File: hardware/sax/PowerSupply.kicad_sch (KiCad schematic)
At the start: 8 parts, among them U1201 TPSM33625

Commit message: Update library
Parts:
- C1201: footprint Capacitor_SMD:C_1210_3225Metric -> V2_Capacitor_SMD:C_1210; symbol Device:C_Small -> V2_Device:C_1210_10u; Manufacturer (none) -> TDK; Mouser (none) -> 810-CNA6P1X7R1H106K2; Product (none) -> CNA6P1X7R1H106K250AE; Voltage (none) -> 50V
- C1202: footprint Capacitor_SMD:C_0603_1608Metric -> V2_Capacitor_SMD:C_0603; symbol Device:C_Small -> V2_Device:C_0603_0u1; Manufacturer (none) -> TDK; Mouser (none) -> 810-CGA3E2X7R1H104MA; Product (none) -> CGA3E2X7R1H104M080AA
- C1203, C1204: footprint Capacitor_SMD:C_1210_3225Metric -> V2_Capacitor_SMD:C_1210; symbol Device:C_Small -> V2_Device:C_1210_22u; Manufacturer (none) -> TDK; Mouser (none) -> 810-CGA6P3X7R1E226M5; Product (none) -> CGA6P3X7R1E226M250AE; Voltage (none) -> 25V
- C1205: footprint Capacitor_SMD:C_0603_1608Metric -> V2_Capacitor_SMD:C_0603; symbol Device:C_Small -> V2_Device:C_0603_1u; Manufacturer (none) -> YAGEO; Mouser (none) -> 603-CC603KRX7R9BB105; Product (none) -> CC0603KRX7R9BB105
- R1201: footprint Resistor_SMD:R_0603_1608Metric -> V2_Resistor_SMD:R_0603; symbol Device:R_Small -> V2_Device:R_0603_40k2; Manufacturer (none) -> Vishay; Mouser (none) -> 71-RCS060340K2FKEA; Product (none) -> RCS060340K2FKEA; Rating (none) -> 500mW
- R1202: footprint Resistor_SMD:R_0603_1608Metric -> V2_Resistor_SMD:R_0603; symbol Device:R_Small -> V2_Device:R_0603_10k; Manufacturer (none) -> Vishay; Mouser (none) -> 71-CRCW060310K0FKEAC; Product (none) -> CRCW060310K0FKEAC; Rating (none) -> 100mW
- U1201: Manufacturer (none) -> Texas Instruments; Mouser (none) -> 595-TPSM33625RDNR; Product (none) -> TPSM33625RDNR

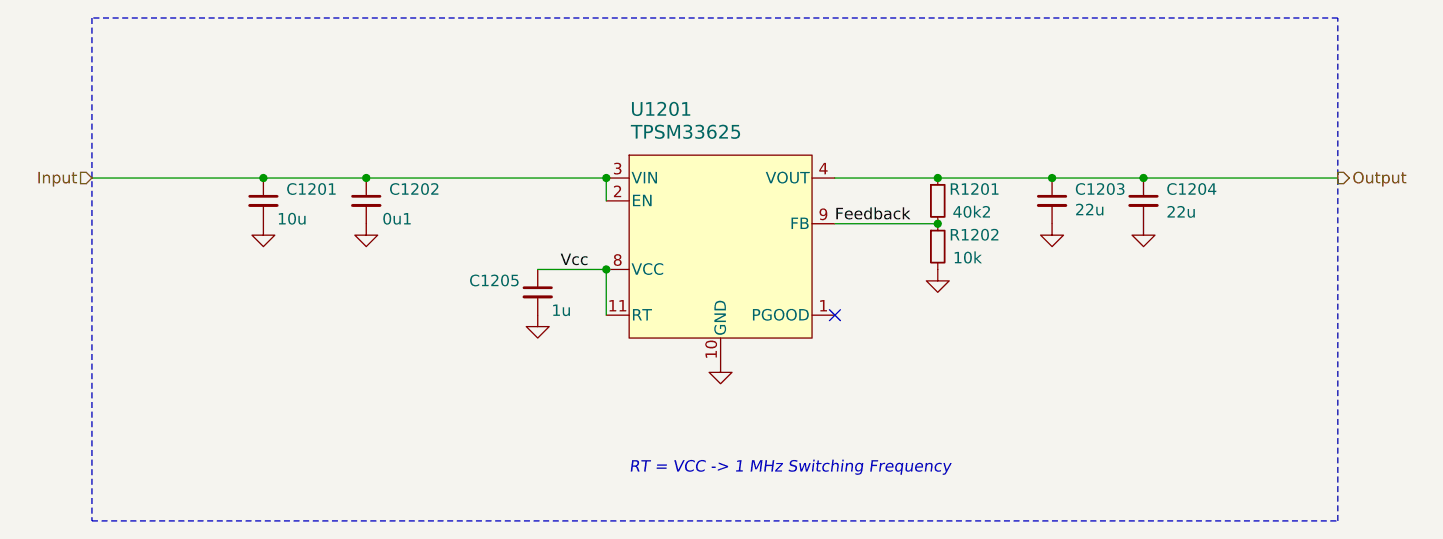
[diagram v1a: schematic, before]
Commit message: Replace Order_Number
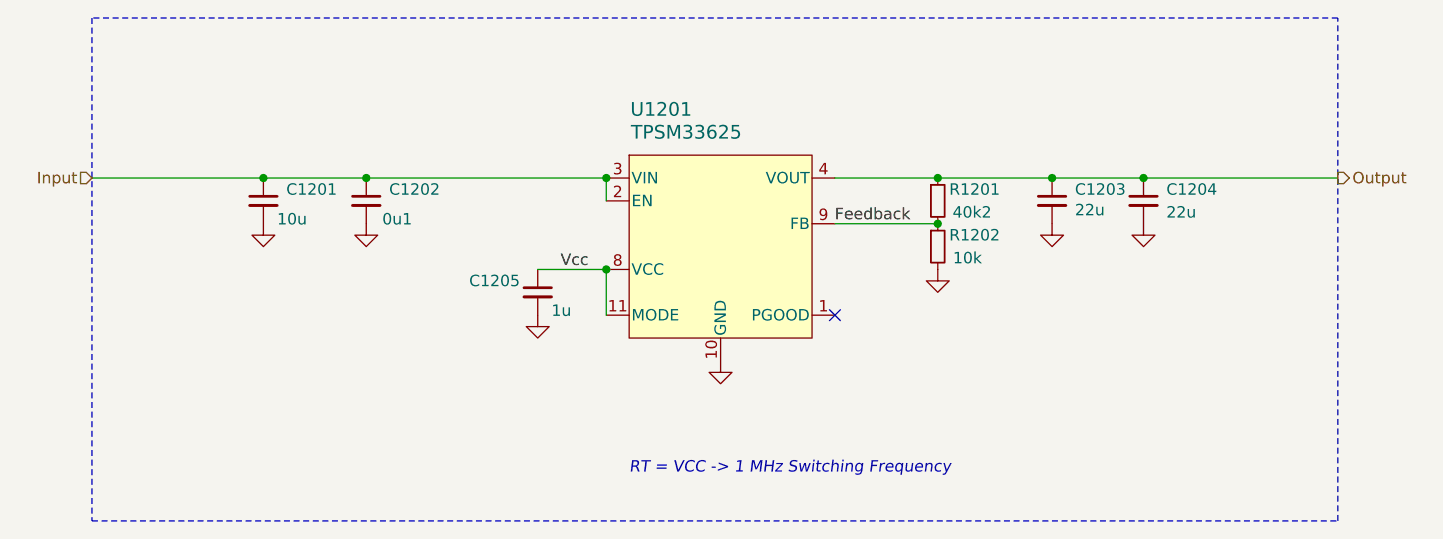
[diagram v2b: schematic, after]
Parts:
- C1201: Rating (none) -> 50V; Voltage 50V -> (none)
- C1202: Rating (none) -> 50V
- C1203, C1204: Rating (none) -> 25V; Voltage 25V -> (none)
- C1205: Manufacturer YAGEO -> TDK; Mouser 603-CC603KRX7R9BB105 -> 810-CGA3E3X7R1H105K0; Product CC0603KRX7R9BB105 -> CGA3E3X7R1H105K080AB; Rating (none) -> 50V
- U1201: footprint V2_Converter_DCDC:TPSM33625 -> V2_Converter_DCDC:QFN-11; symbol V2_Converter_DCDC:TPSM33625 -> V2_Converter_DCDC:TPSM33625RDNR; Rating (none) -> 2.5A
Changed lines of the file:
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@@
 	)
 	(symbol
-		(lib_id "V2_Converter_DCDC:TPSM33625")
+		(lib_id "V2_Converter_DCDC:TPSM33625RDNR")
 		(at 148.59 102.87 0)
 		(unit 1)
@@
 			)
 		)
-		(property "Footprint" "V2_Converter_DCDC:TPSM33625"
+		(property "Footprint" "V2_Converter_DCDC:QFN-11"
 			(at 148.59 118.11 0)
 			(effects
@@
 			)
 		)
-		(property "Datasheet" "https://www.ti.com/lit/ds/symlink/tpsm33625.pdf"
+		(property "Datasheet" ""
 			(at 153.67 118.11 0)
 			(effects
@@
 			)
 		)
+		(property "Rating" "2.5A"
+			(at 148.59 153.67 0)
+			(effects
+				(font
+					(size 1.27 1.27)
+				)
+				(hide yes)
+			)
+		)
 		(pin "1"
 		)
@@
 			)
 		)
+		(property "Rating" "50V"
+			(at 109.22 120.65 0)
+			(effects
+				(font
+					(size 1.27 1.27)
+				)
+				(hide yes)
+			)
+		)
 		(pin "1"
 		)
@@
 			)
 		)
-		(property "Voltage" "25V"
-			(at 195.58 118.11 0)
-			(effects
-				(font
-					(size 1.27 1.27)
-				)
-				(hide yes)
-			)
-		)
 		(property "Product" "CGA6P3X7R1E226M250AE"
 			(at 195.58 115.57 0)
@@
 			)
 		)
+		(property "Rating" "25V"
+			(at 195.58 118.11 0)
+			(effects
+				(font
+					(size 1.27 1.27)
+				)
+				(hide yes)
+			)
+		)
 		(pin "1"
 		)
@@
 			)
 		)
-		(property "Description" "Power symbol creates a global label with name \"GND\" , ground"
+		(property "Description" ""
 			(at 185.42 100.33 0)
 			(effects
@@
 			)
 		)
-		(property "Description" "Power symbol creates a global label with name \"GND\" , ground"
+		(property "Description" ""
 			(at 195.58 100.33 0)
 			(effects
@@
 			)
 		)
-		(property "Description" "Power symbol creates a global label with name \"GND\" , ground"
+		(property "Description" ""
 			(at 97.79 100.33 0)
 			(effects
@@
 			)
 		)
-		(property "Description" "Power symbol creates a global label with name \"GND\" , ground"
+		(property "Description" ""
 			(at 172.72 105.41 0)
 			(effects
@@
 			)
 		)
-		(property "Description" "Power symbol creates a global label with name \"GND\" , ground"
+		(property "Description" ""
 			(at 109.22 100.33 0)
 			(effects
@@
 			)
 		)
-		(property "Mouser" "603-CC603KRX7R9BB105"
+		(property "Mouser" "810-CGA3E3X7R1H105K0"
 			(at 128.27 128.27 0)
 			(effects
@@
 			)
 		)
-		(property "Product" "CC0603KRX7R9BB105"
+		(property "Product" "CGA3E3X7R1H105K080AB"
 			(at 128.27 125.73 0)
 			(effects
@@
 			)
 		)
-		(property "Manufacturer" "YAGEO"
+		(property "Manufacturer" "TDK"
 			(at 128.27 123.19 0)
+			(effects
+				(font
+					(size 1.27 1.27)
+				)
+				(hide yes)
+			)
+		)
+		(property "Rating" "50V"
+			(at 128.27 130.81 0)
 			(effects
 				(font
@@
 			)
 		)
-		(property "Voltage" "25V"
-			(at 185.42 118.11 0)
-			(effects
-				(font
-					(size 1.27 1.27)
-				)
-				(hide yes)
-			)
-		)
 		(property "Product" "CGA6P3X7R1E226M250AE"
 			(at 185.42 115.57 0)
@@
 			)
 		)
+		(property "Rating" "25V"
+			(at 185.42 118.11 0)
+			(effects
+				(font
+					(size 1.27 1.27)
+				)
+				(hide yes)
+			)
+		)
 		(pin "1"
 		)
@@
 			)
 		)
-		(property "Description" "Power symbol creates a global label with name \"GND\" , ground"
+		(property "Description" ""
 			(at 128.27 110.49 0)
 			(effects
@@
 			)
 		)
-		(property "Description" "Power symbol creates a global label with name \"GND\" , ground"
+		(property "Description" ""
 			(at 148.59 115.57 0)
 			(effects
@@
 			)
 		)
-		(property "Voltage" "50V"
+		(property "Rating" "50V"
 			(at 97.79 118.11 0)
 			(effects

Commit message: Update Library
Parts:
- C1201: symbol V2_Device:C_1210_10u -> V2_Capacitor:1210_10u
- C1202: symbol V2_Device:C_0603_0u1 -> V2_Capacitor:0603_0u1
- C1203, C1204: value 22u -> 10u; symbol V2_Device:C_1210_22u -> V2_Capacitor:1210_22u
- C1205: symbol V2_Device:C_0603_1u -> V2_Capacitor:0603_1u
- R1201: symbol V2_Device:R_0603_40k2 -> V2_Resistor:0603_40k2
- R1202: symbol V2_Device:R_0603_10k -> V2_Resistor:0603_10k
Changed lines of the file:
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@@
 	)
 	(symbol
-		(lib_id "V2_Device:C_0603_0u1")
+		(lib_id "V2_Capacitor:0603_0u1")
 		(at 109.22 97.79 0)
 		(unit 1)
@@
 	)
 	(symbol
-		(lib_id "V2_Device:C_1210_22u")
+		(lib_id "V2_Capacitor:1210_22u")
 		(at 195.58 97.79 0)
 		(unit 1)
@@
 			)
 		)
-		(property "Value" "22u"
+		(property "Value" "10u"
 			(at 198.12 99.06 0)
 			(effects
@@
 	)
 	(symbol
-		(lib_id "V2_Device:R_0603_40k2")
+		(lib_id "V2_Resistor:0603_40k2")
 		(at 172.72 97.79 0)
 		(unit 1)
@@
 		(on_board yes)
 		(dnp no)
-		(property "Reference" "#PWR01203"
+		(property "Reference" "#PWR1203"
 			(at 185.42 106.68 0)
 			(effects
@@
 			(project "sax"
 				(path "/6c8448b4-b04d-47e1-934e-e40cbe27a7be/095cddf1-6522-4d3b-885d-b21acd91d0c6"
-					(reference "#PWR01203")
+					(reference "#PWR1203")
 					(unit 1)
 				)
@@
 		(on_board yes)
 		(dnp no)
-		(property "Reference" "#PWR01204"
+		(property "Reference" "#PWR1204"
 			(at 195.58 106.68 0)
 			(effects
@@
 			(project "sax"
 				(path "/6c8448b4-b04d-47e1-934e-e40cbe27a7be/095cddf1-6522-4d3b-885d-b21acd91d0c6"
-					(reference "#PWR01204")
+					(reference "#PWR1204")
 					(unit 1)
 				)
@@
 		(on_board yes)
 		(dnp no)
-		(property "Reference" "#PWR01201"
+		(property "Reference" "#PWR1201"
 			(at 97.79 106.68 0)
 			(effects
@@
 			(project "sax"
 				(path "/6c8448b4-b04d-47e1-934e-e40cbe27a7be/095cddf1-6522-4d3b-885d-b21acd91d0c6"
-					(reference "#PWR01201")
+					(reference "#PWR1201")
 					(unit 1)
 				)
@@
 		(on_board yes)
 		(dnp no)
-		(property "Reference" "#PWR01205"
+		(property "Reference" "#PWR1205"
 			(at 172.72 111.76 0)
 			(effects
@@
 			(project "sax"
 				(path "/6c8448b4-b04d-47e1-934e-e40cbe27a7be/095cddf1-6522-4d3b-885d-b21acd91d0c6"
-					(reference "#PWR01205")
+					(reference "#PWR1205")
 					(unit 1)
 				)
@@
 		(on_board yes)
 		(dnp no)
-		(property "Reference" "#PWR01202"
+		(property "Reference" "#PWR1202"
 			(at 109.22 106.68 0)
 			(effects
@@
 			(project "sax"
 				(path "/6c8448b4-b04d-47e1-934e-e40cbe27a7be/095cddf1-6522-4d3b-885d-b21acd91d0c6"
-					(reference "#PWR01202")
-					(unit 1)
-				)
-			)
-		)
-	)
-	(symbol
-		(lib_id "V2_Device:C_0603_1u")
+					(reference "#PWR1202")
+					(unit 1)
+				)
+			)
+		)
+	)
+	(symbol
+		(lib_id "V2_Capacitor:0603_1u")
 		(at 128.27 107.95 0)
 		(unit 1)
@@
 	)
 	(symbol
-		(lib_id "V2_Device:C_1210_22u")
+		(lib_id "V2_Capacitor:1210_22u")
 		(at 185.42 97.79 0)
 		(unit 1)
@@
 			)
 		)
-		(property "Value" "22u"
+		(property "Value" "10u"
 			(at 187.96 98.806 0)
 			(effects
@@
 		(on_board yes)
 		(dnp no)
-		(property "Reference" "#PWR01206"
+		(property "Reference" "#PWR1206"
 			(at 128.27 116.84 0)
 			(effects
@@
 			(project "sax"
 				(path "/6c8448b4-b04d-47e1-934e-e40cbe27a7be/095cddf1-6522-4d3b-885d-b21acd91d0c6"
-					(reference "#PWR01206")
-					(unit 1)
-				)
-			)
-		)
-	)
-	(symbol
-		(lib_id "V2_Device:R_0603_10k")
+					(reference "#PWR1206")
+					(unit 1)
+				)
+			)
+		)
+	)
+	(symbol
+		(lib_id "V2_Resistor:0603_10k")
 		(at 172.72 102.87 0)
 		(unit 1)
@@
 		(on_board yes)
 		(dnp no)
-		(property "Reference" "#PWR01207"
+		(property "Reference" "#PWR1207"
 			(at 148.59 121.92 0)
 			(effects
@@
 			(project "sax"
 				(path "/6c8448b4-b04d-47e1-934e-e40cbe27a7be/095cddf1-6522-4d3b-885d-b21acd91d0c6"
-					(reference "#PWR01207")
-					(unit 1)
-				)
-			)
-		)
-	)
-	(symbol
-		(lib_id "V2_Device:C_1210_10u")
+					(reference "#PWR1207")
+					(unit 1)
+				)
+			)
+		)
+	)
+	(symbol
+		(lib_id "V2_Capacitor:1210_10u")
 		(at 97.79 97.79 0)
 		(unit 1)

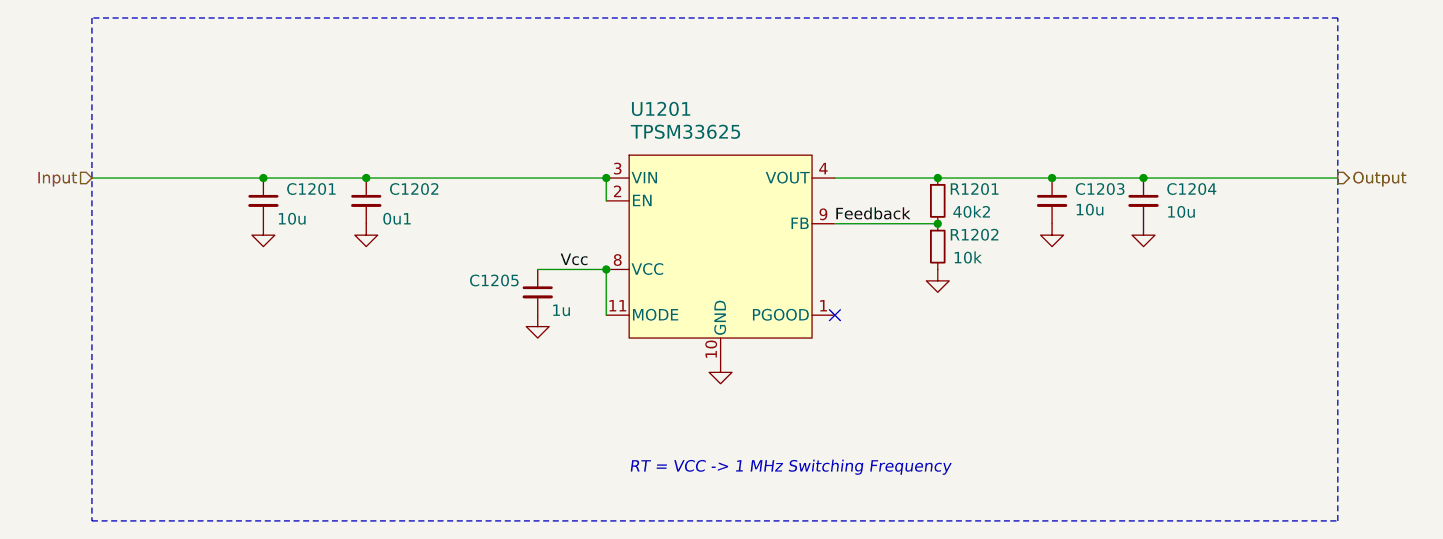
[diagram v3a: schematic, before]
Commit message: sax2 -> sax
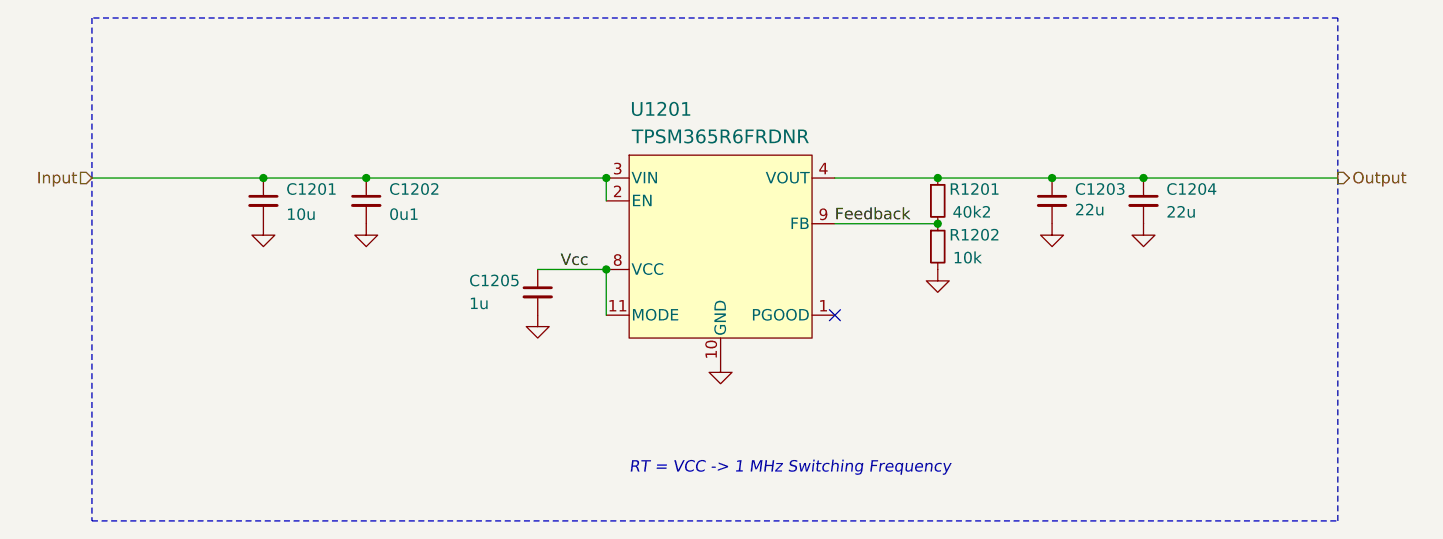
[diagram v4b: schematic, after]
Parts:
- C1203, C1204: value 10u -> 22u
- U1201: value TPSM33625 -> TPSM365R6FRDNR; symbol V2_Converter_DCDC:TPSM33625RDNR -> V2_Converter_DCDC:TPSM365R6FRDNR; Mouser 595-TPSM33625RDNR -> 595-TPSM365R6FRDNR; Product TPSM33625RDNR -> TPSM365R6FRDNR; Rating 2.5A -> 600mA
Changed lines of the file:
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@@
 	)
 	(symbol
-		(lib_id "V2_Converter_DCDC:TPSM33625RDNR")
+		(lib_id "V2_Converter_DCDC:TPSM365R6FRDNR")
 		(at 148.59 102.87 0)
 		(unit 1)
@@
 			)
 		)
-		(property "Value" "TPSM33625"
-			(at 144.78 90.17 0)
+		(property "Value" "TPSM365R6FRDNR"
+			(at 148.59 90.678 0)
 			(effects
 				(font
@@
 			)
 		)
-		(property "Mouser" "595-TPSM33625RDNR"
+		(property "Mouser" "595-TPSM365R6FRDNR"
 			(at 148.59 151.13 0)
 			(effects
@@
 			)
 		)
-		(property "Product" "TPSM33625RDNR"
+		(property "Product" "TPSM365R6FRDNR"
 			(at 148.59 148.59 0)
 			(effects
@@
 			)
 		)
-		(property "Rating" "2.5A"
+		(property "Rating" "600mA"
 			(at 148.59 153.67 0)
 			(effects
@@
 		)
 		(instances
-			(project "sax"
+			(project "sax2"
 				(path "/6c8448b4-b04d-47e1-934e-e40cbe27a7be/095cddf1-6522-4d3b-885d-b21acd91d0c6"
 					(reference "U1201")
@@
 		)
 		(property "Value" "0u1"
-			(at 110.998 99.822 0)
+			(at 111.76 99.314 0)
 			(effects
 				(font
@@
 		)
 		(instances
-			(project "sax"
+			(project "sax2"
 				(path "/6c8448b4-b04d-47e1-934e-e40cbe27a7be/095cddf1-6522-4d3b-885d-b21acd91d0c6"
 					(reference "C1202")
@@
 			)
 		)
-		(property "Value" "10u"
+		(property "Value" "22u"
 			(at 198.12 99.06 0)
 			(effects
@@
 		)
 		(instances
-			(project "sax"
+			(project "sax2"
 				(path "/6c8448b4-b04d-47e1-934e-e40cbe27a7be/095cddf1-6522-4d3b-885d-b21acd91d0c6"
 					(reference "C1204")
@@
 		)
 		(instances
-			(project "sax"
+			(project "sax2"
 				(path "/6c8448b4-b04d-47e1-934e-e40cbe27a7be/095cddf1-6522-4d3b-885d-b21acd91d0c6"
 					(reference "R1201")
@@
 		)
 		(instances
-			(project "sax"
+			(project "sax2"
 				(path "/6c8448b4-b04d-47e1-934e-e40cbe27a7be/095cddf1-6522-4d3b-885d-b21acd91d0c6"
 					(reference "#PWR1203")
@@
 		)
 		(instances
-			(project "sax"
+			(project "sax2"
 				(path "/6c8448b4-b04d-47e1-934e-e40cbe27a7be/095cddf1-6522-4d3b-885d-b21acd91d0c6"
 					(reference "#PWR1204")
@@
 		)
 		(instances
-			(project "sax"
+			(project "sax2"
 				(path "/6c8448b4-b04d-47e1-934e-e40cbe27a7be/095cddf1-6522-4d3b-885d-b21acd91d0c6"
 					(reference "#PWR1201")
@@
 		)
 		(instances
-			(project "sax"
+			(project "sax2"
 				(path "/6c8448b4-b04d-47e1-934e-e40cbe27a7be/095cddf1-6522-4d3b-885d-b21acd91d0c6"
 					(reference "#PWR1205")
@@
 		)
 		(instances
-			(project "sax"
+			(project "sax2"
 				(path "/6c8448b4-b04d-47e1-934e-e40cbe27a7be/095cddf1-6522-4d3b-885d-b21acd91d0c6"
 					(reference "#PWR1202")
@@
 		)
 		(property "Value" "1u"
-			(at 129.794 109.982 0)
+			(at 120.65 109.22 0)
 			(effects
 				(font
@@
 		)
 		(instances
-			(project "sax"
+			(project "sax2"
 				(path "/6c8448b4-b04d-47e1-934e-e40cbe27a7be/095cddf1-6522-4d3b-885d-b21acd91d0c6"
 					(reference "C1205")
@@
 			)
 		)
-		(property "Value" "10u"
+		(property "Value" "22u"
 			(at 187.96 98.806 0)
 			(effects
@@
 		)
 		(instances
-			(project "sax"
+			(project "sax2"
 				(path "/6c8448b4-b04d-47e1-934e-e40cbe27a7be/095cddf1-6522-4d3b-885d-b21acd91d0c6"
 					(reference "C1203")
@@
 		)
 		(instances
-			(project "sax"
+			(project "sax2"
 				(path "/6c8448b4-b04d-47e1-934e-e40cbe27a7be/095cddf1-6522-4d3b-885d-b21acd91d0c6"
 					(reference "#PWR1206")
@@
 		)
 		(instances
-			(project "sax"
+			(project "sax2"
 				(path "/6c8448b4-b04d-47e1-934e-e40cbe27a7be/095cddf1-6522-4d3b-885d-b21acd91d0c6"
 					(reference "R1202")
@@
 		)
 		(instances
-			(project "sax"
+			(project "sax2"
 				(path "/6c8448b4-b04d-47e1-934e-e40cbe27a7be/095cddf1-6522-4d3b-885d-b21acd91d0c6"
 					(reference "#PWR1207")
@@
 		)
 		(property "Value" "10u"
-			(at 99.314 99.822 0)
+			(at 100.33 99.314 0)
 			(effects
 				(font
@@
 		)
 		(instances
-			(project "sax"
+			(project "sax2"
 				(path "/6c8448b4-b04d-47e1-934e-e40cbe27a7be/095cddf1-6522-4d3b-885d-b21acd91d0c6"
 					(reference "C1201")

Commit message: Refresh
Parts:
- C1201: Mouser 810-CNA6P1X7R1H106K2 -> 810-CNC6P1X7R1H106K2; Product CNA6P1X7R1H106K250AE -> CNC6P1X7R1H106K250AE
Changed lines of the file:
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@@
 			)
 		)
-		(property "Mouser" "810-CNA6P1X7R1H106K2"
+		(property "Mouser" "810-CNC6P1X7R1H106K2"
 			(at 97.79 120.65 0)
 			(show_name yes)
@@
 			)
 		)
-		(property "Product" "CNA6P1X7R1H106K250AE"
+		(property "Product" "CNC6P1X7R1H106K250AE"
 			(at 97.79 115.57 0)
 			(show_name yes)

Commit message: KiCad 10
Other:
- company: +5V -> Versio Duo
